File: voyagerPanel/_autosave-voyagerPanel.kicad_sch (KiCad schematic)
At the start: 22 parts, among them J1 USB_C_Receptacle_USB2.0_16P, J2 Conn_01x02_Pin, U1 ESP32-S3-MINI-1, U2 MCP1700x-330xxMB, U4 TP4056-42-ESOP8

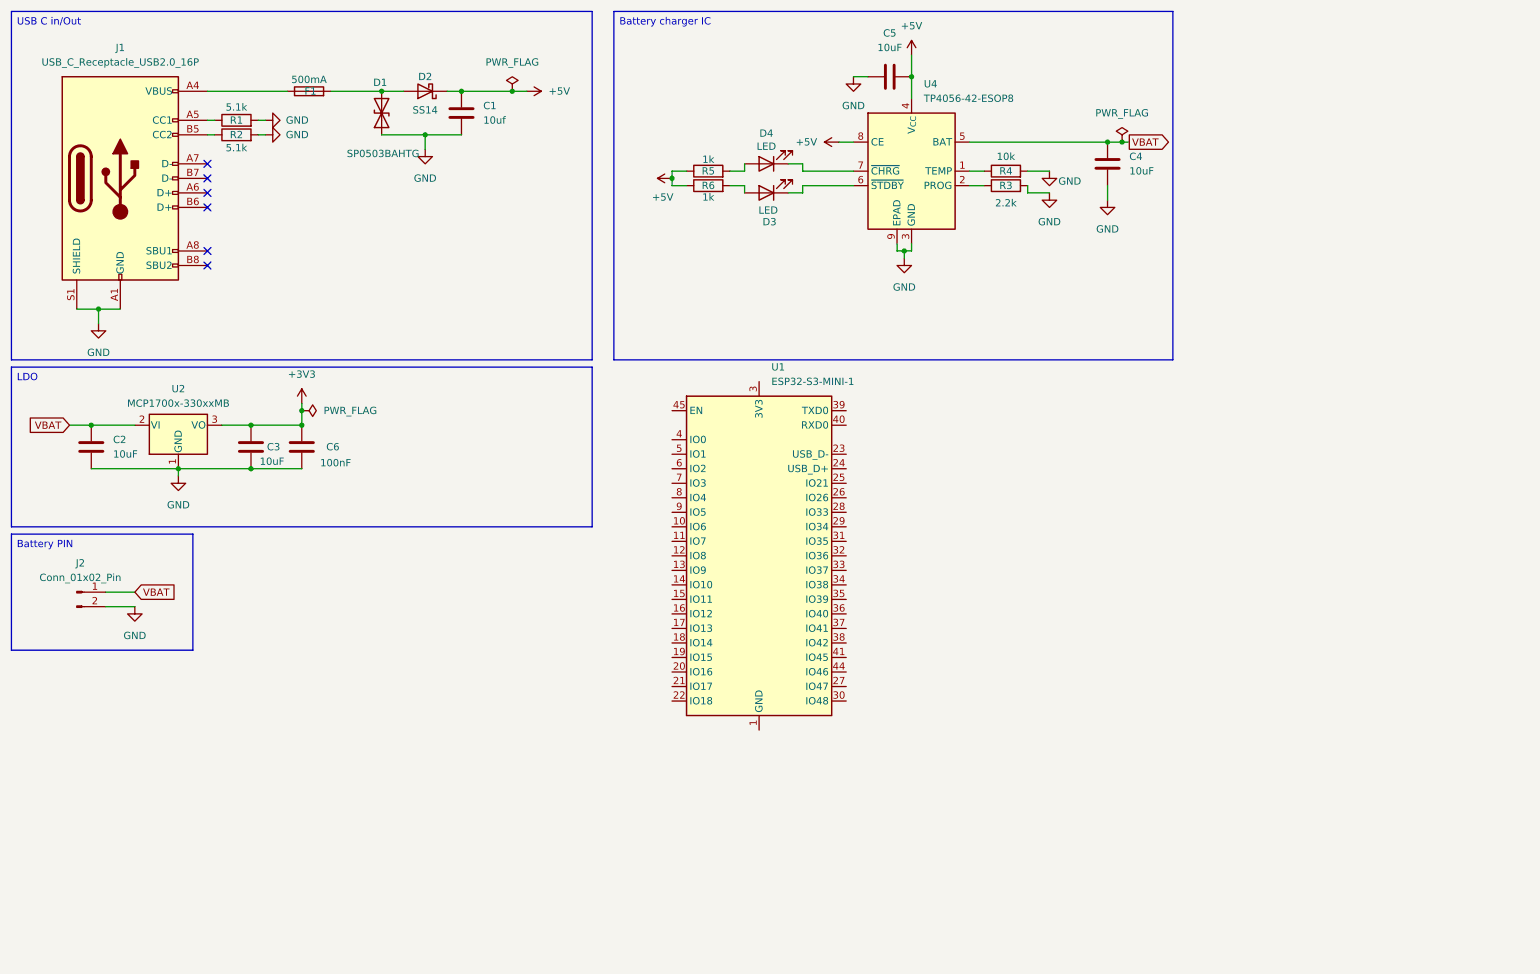
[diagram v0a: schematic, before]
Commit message: Finished schematic creating pcb
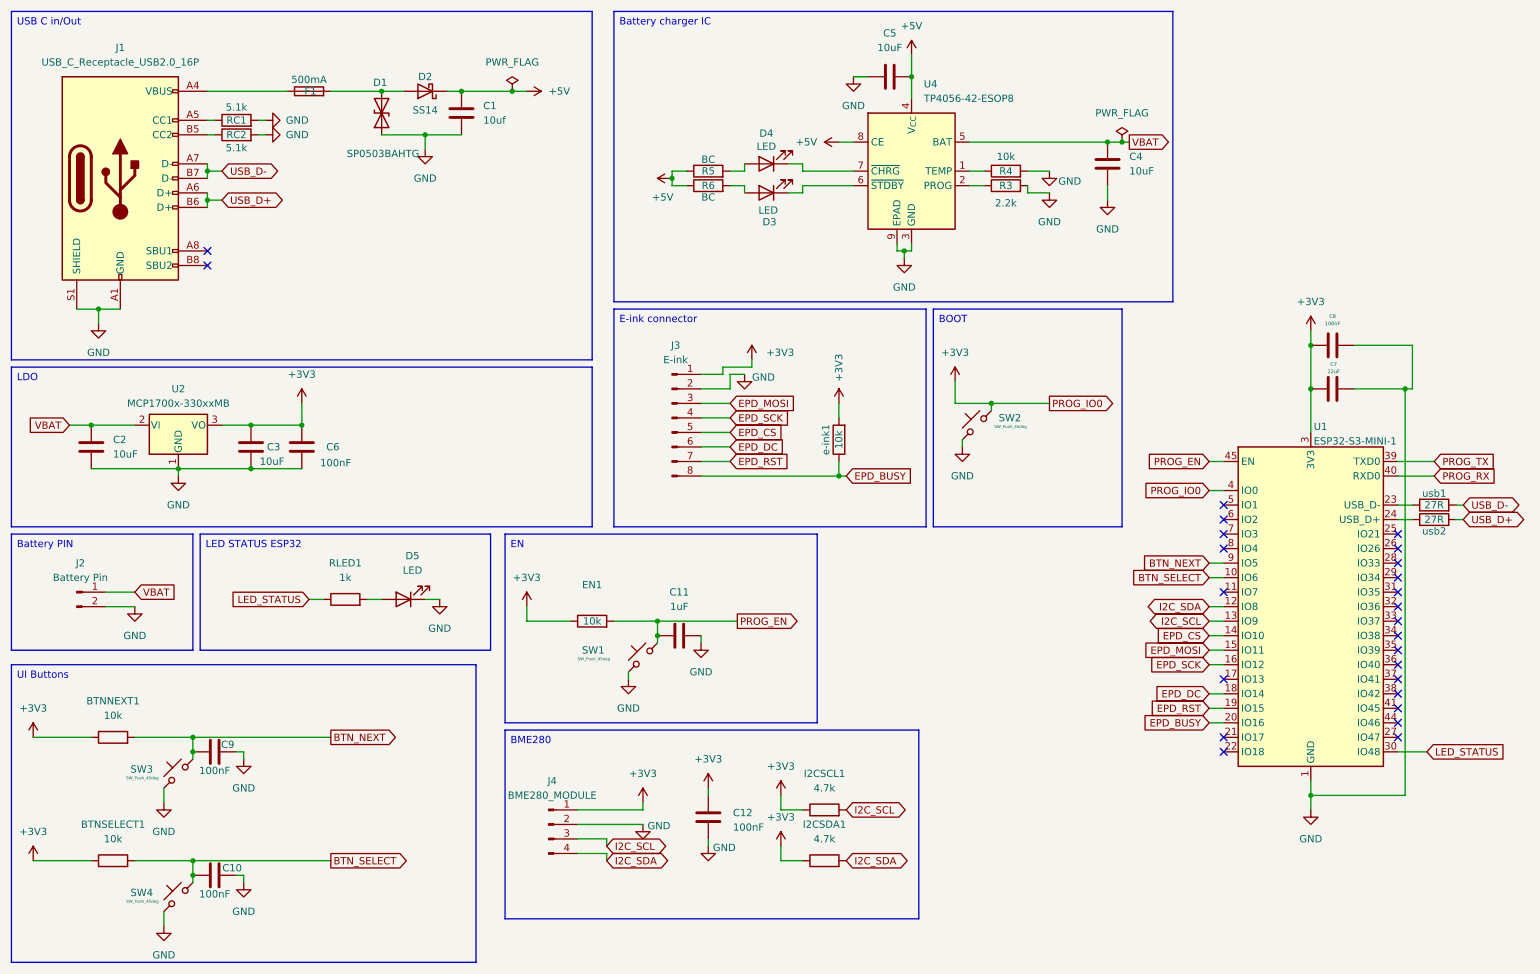
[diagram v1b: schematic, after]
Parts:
- added BTNNEXT1, BTNSELECT1, EN1, e-ink1: 10k, Resistor_SMD:R_0805_2012Metric, symbol Device:R
- added C10, C12, C8, C9: 100nF, Capacitor_SMD:C_0805_2012Metric, symbol Device:C
- added C11: 1uF, Capacitor_SMD:C_0805_2012Metric, symbol Device:C
- added C7: 22uF, Capacitor_SMD:C_0805_2012Metric, symbol Device:C
- added D5: LED, LED_SMD:LED_0805_2012Metric, symbol Device:LED
- added I2CSCL1, I2CSDA1: 4.7k, Resistor_SMD:R_0805_2012Metric, symbol Device:R
- added J3: E-ink, Connector_PinHeader_2.54mm:PinHeader_1x08_P2.54mm_Vertical, symbol Connector:Conn_01x08_Pin
- added J4: BME280_MODULE, Connector_PinHeader_2.54mm:PinHeader_1x04_P2.54mm_Vertical, symbol Connector:Conn_01x04_Pin
- added RLED1: 1k, Resistor_SMD:R_0805_2012Metric, symbol Device:R
- added SW1, SW2, SW3, SW4: SW_Push_45deg, Button_Switch_SMD:SW_SPST_TL3342, symbol Switch:SW_Push_45deg
- added usb1, usb2: 27R, Resistor_SMD:R_0805_2012Metric, symbol Device:R
- C1, C2, C3, C4, C5, C6: footprint (none) -> Capacitor_SMD:C_0805_2012Metric
- D1: footprint (none) -> Package_TO_SOT_SMD:SOT-363_SC-70-6
- D3, D4: footprint (none) -> LED_SMD:LED_0805_2012Metric
- F1: footprint (none) -> Fuse:Fuse_1206_3216Metric
- J1: footprint (none) -> Connector_USB:USB_C_Receptacle_HRO_TYPE-C-31-M-12
- J2: value Conn_01x02_Pin -> Battery Pin; footprint (none) -> Connector_JST:JST_PH_B2B-PH-K_1x02_P2.00mm_Vertical
- R3, R4: footprint (none) -> Resistor_SMD:R_0805_2012Metric
- R5, R6: value 1k -> BC; footprint (none) -> Resistor_SMD:R_0805_2012Metric
- RC1: renamed from R1; footprint (none) -> Resistor_SMD:R_0805_2012Metric
- RC2: renamed from R2; footprint (none) -> Resistor_SMD:R_0805_2012Metric
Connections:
- net +3V3: now also U1.3 (3V3), U1.4 (IO0), BTNNEXT1.1, BTNSELECT1.1, C12.1, C7.1, C8.1, EN1.1, I2CSCL1.1, I2CSDA1.1, J3.1 (Pin_1), J4.1 (Pin_1), SW2.2, e-ink1.2
- net GND: now also U1.1 (GND), U1.2 (GND), U1.42 (GND), U1.43 (GND), U1.46 (GND), U1.47 (GND), U1.48 (GND), U1.49 (GND), U1.50 (GND), U1.51 (GND), U1.52 (GND), U1.53 (GND), U1.54 (GND), U1.55 (GND), U1.56 (GND), U1.57 (GND), U1.58 (GND), U1.59 (GND), U1.60 (GND), U1.61 (GND), U1.62 (GND), U1.63 (GND), U1.64 (GND), U1.65 (GND), C10.2, C11.1, C12.2, C7.2, C8.2, C9.2, D5.1 (K), J3.2 (Pin_2), J4.2 (Pin_2), SW1.1, SW2.1, SW3.1, SW4.1
- net BTN_SELECT: now reaches U1.10 (IO6)
- net BTN_SELECT: now also BTNSELECT1.2, C10.1, SW4.2
- net I2C_SDA: now reaches U1.12 (IO8)
- net I2C_SDA: now also I2CSDA1.2, J4.4 (Pin_4)
- net I2C_SCL: now reaches U1.13 (IO9)
- net I2C_SCL: now also I2CSCL1.2, J4.3 (Pin_3)
- net EPD_CS: now reaches U1.14 (IO10)
- net EPD_CS: now also J3.5 (Pin_5)
- net EPD_MOSI: now reaches U1.15 (IO11)
- net EPD_MOSI: now also J3.3 (Pin_3)
- net EPD_SCK: now reaches U1.16 (IO12)
- net EPD_SCK: now also J3.4 (Pin_4)
- net EPD_DC: now reaches U1.18 (IO14)
- net EPD_DC: now also J3.6 (Pin_6)
- net EPD_RST: now reaches U1.19 (IO15)
- net EPD_RST: now also J3.7 (Pin_7)
- net EPD_BUSY: now reaches U1.20 (IO16)
- net EPD_BUSY: now also J3.8 (Pin_8), e-ink1.1
- net at U1.23 (USB_D-): now also usb1.1
- net at U1.24 (USB_D+): now also usb2.1
- net LED_STATUS: now reaches U1.30 (IO48)
- net LED_STATUS: now also RLED1.1
- net PROG_TX: now reaches U1.39 (TXD0)
- net PROG_RX: now reaches U1.40 (RXD0)
- net PROG_EN: now reaches U1.45 (EN)
- net PROG_EN: now also C11.2, EN1.2, SW1.2
- net BTN_NEXT: now reaches U1.9 (IO5)
- net BTN_NEXT: now also BTNNEXT1.2, C9.1, SW3.2
- net USB_D+: now reaches J1.A6 (D+)
- net USB_D+: now also J1.B6 (D+), usb2.2
- net USB_D-: now reaches J1.A7 (D-)
- net USB_D-: now also J1.B7 (D-), usb1.2
- new net: D5.2 (A), RLED1.2
- no-connect marks 6 -> 25
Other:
- moved on the sheet: U1
